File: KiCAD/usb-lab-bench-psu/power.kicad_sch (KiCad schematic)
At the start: 34 parts, among them Q3 NMOS, Q4 NMOS, Q5 NMOS

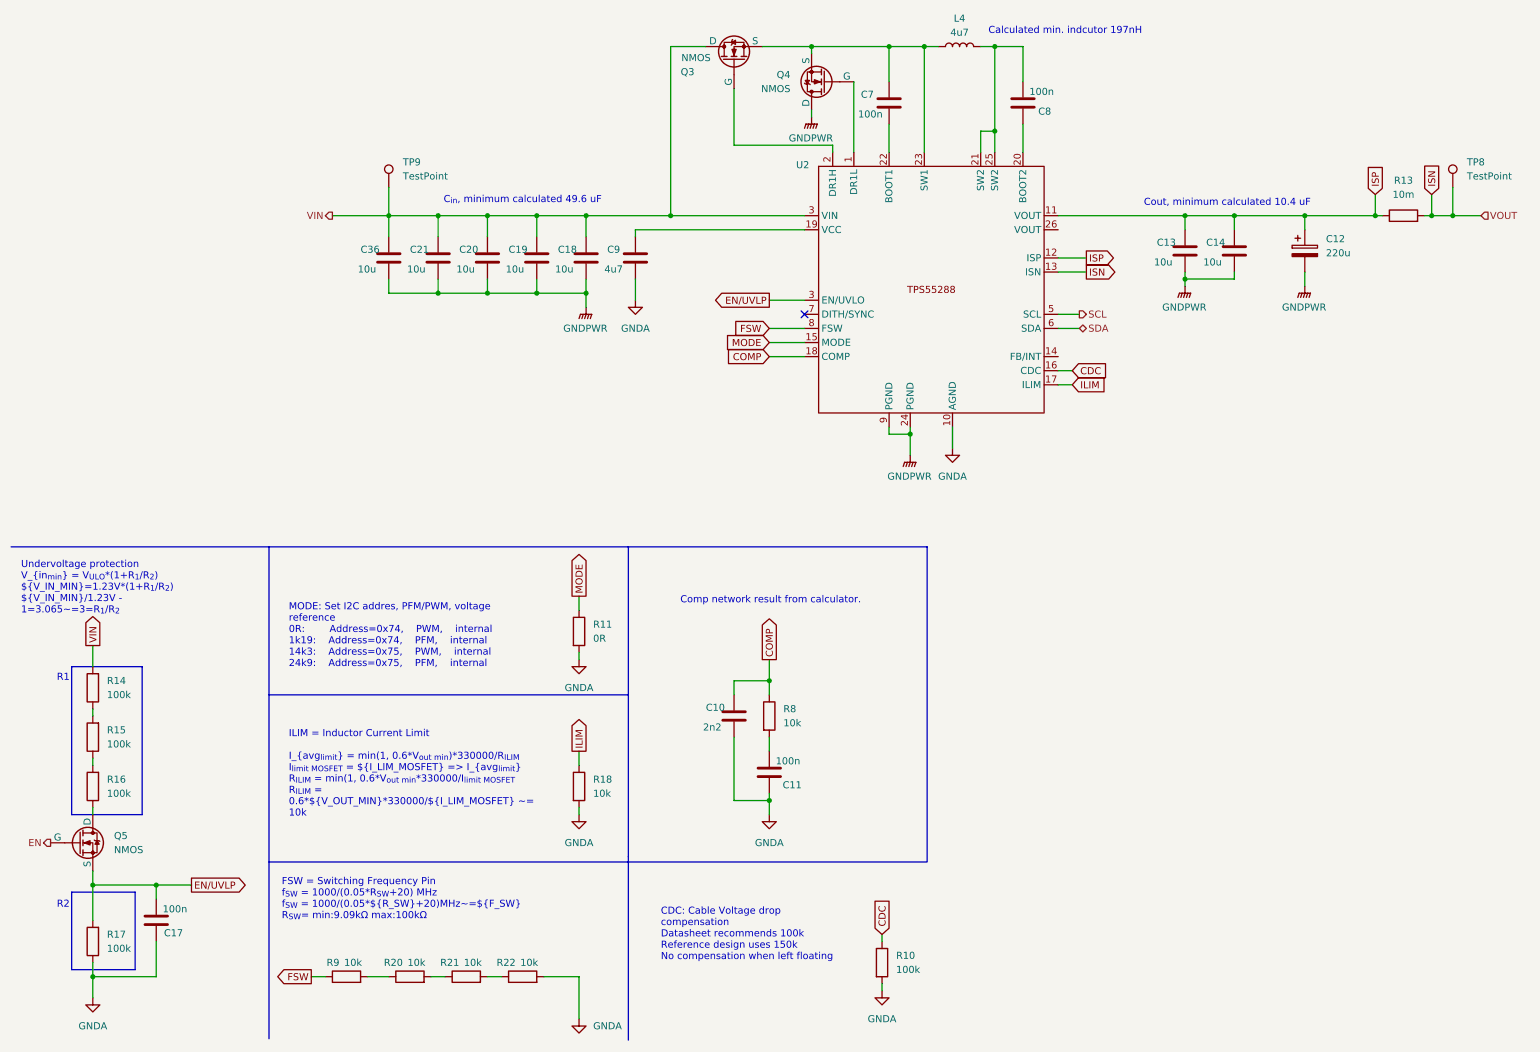
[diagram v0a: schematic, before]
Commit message: Replaced global labels with labels, added measurement circuit, started with io board
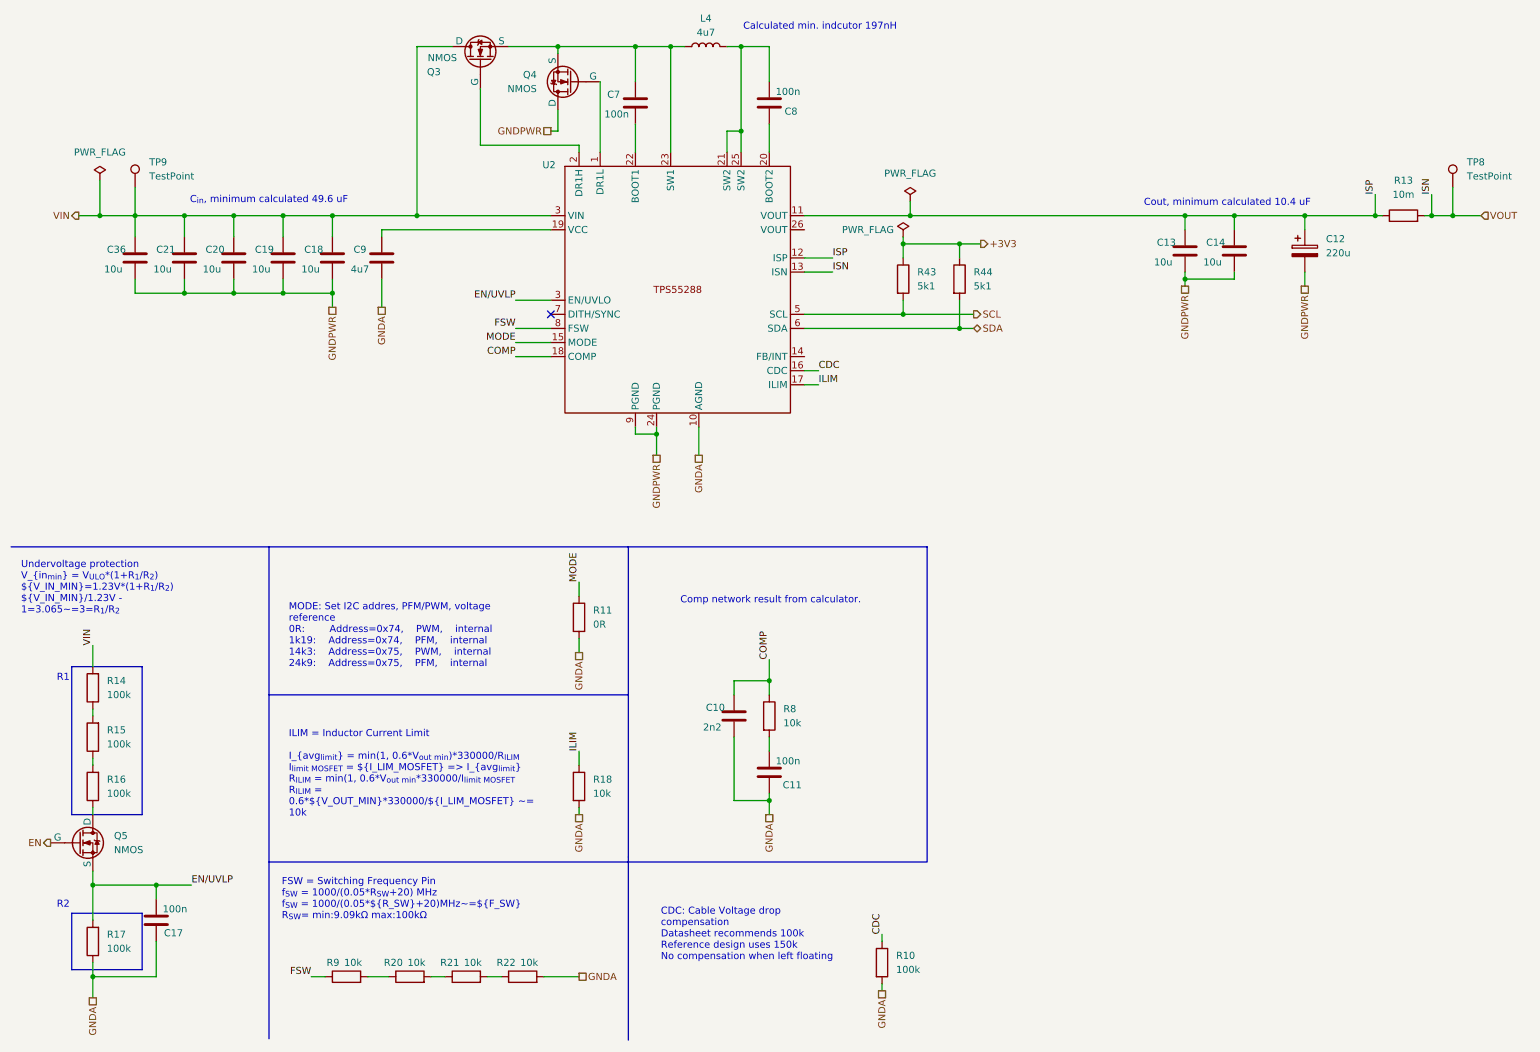
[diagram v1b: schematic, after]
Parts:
- added R43, R44: 5k1, symbol Device:R
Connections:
- net SCL: now also R43.2
- net SDA: now also R44.2
- net ISN renamed VOUT
- new net +3V3: R43.1, R44.1
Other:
- moved on the sheet: C18, C19, C20, C21, C36, C7, C8, C9, L4, Q3, Q4, R11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
